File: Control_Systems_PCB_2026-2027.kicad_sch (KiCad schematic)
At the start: 13 parts, among them U1 STM32F446VETx, U3 MS5611-01BA

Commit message: fix(schematic): fixed the pin outs
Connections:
- net SPI2_CLK: now also U1.64 (PC7); no longer U1.52 (PB13)
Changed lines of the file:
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@@
+	(wire
+		(pts
+			(xy 124.46 160.02) (xy 129.54 160.02)
+		)
+		(stroke
+			(width 0)
+			(type default)
+		)
+	)
 	(wire
 		(pts
@@
 		(pts
 			(xy 99.06 48.26) (xy 101.6 48.26)
-		)
-		(stroke
-			(width 0)
-			(type default)
-		)
-	)
-	(wire
-		(pts
-			(xy 124.46 132.08) (xy 129.54 132.08)
 		)
 		(stroke
@@
 		)
 	)
-	(label "SPI2_CLK"
-		(at 129.54 132.08 0)
-		(effects
-			(font
-				(size 1.27 1.27)
-			)
-			(justify left bottom)
-		)
-	)
 	(label "SPI2_MISO"
 		(at 236.855 36.195 270)
@@
 		)
 	)
+	(label "SPI2_CLK"
+		(at 129.54 160.02 0)
+		(effects
+			(font
+				(size 1.27 1.27)
+			)
+			(justify left bottom)
+		)
+	)

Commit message: fix(schematic): applied PCB best practices + suggested changes)
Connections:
- net SSM renamed PD10_CS
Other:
- moved on the sheet: C10, U3

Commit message: feat: add usb-c recepticle (🤞 it's atleast somewhat correct)
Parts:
- added C11: 10n, symbol Device:C
- added C12: 100n, symbol Device:C
- added J1: USB_C_Receptacle_USB2.0_16P, symbol Connector:USB_C_Receptacle_USB2.0_16P
- added R1, R2: 5.1K, symbol Device:R
- added U2: USBLC6-2SC6, Package_TO_SOT_SMD:SOT-23-6, symbol Power_Protection:USBLC6-2SC6
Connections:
- net GND: now also C11.2, C12.2, J1.A1 (GND), J1.A12 (GND), J1.B1 (GND), J1.B12 (GND), J1.SH (SHIELD), R1.1, R2.2, U2.2 (GND)
- net PD10_CS: now also U1.18 (PC3); no longer U1.55 (PD8)
- net SPI2_MISO: now also U1.17 (PC2); no longer U1.53 (PB14)
- net SPI2_MOSI: now also U1.16 (PC1); no longer U1.54 (PB15)
- new net: J1.A5 (CC1), R1.2
- new net: J1.B5 (CC2), R2.1
- new net +5V: C11.1, C12.1, J1.A4 (VBUS), J1.A9 (VBUS), J1.B4 (VBUS), J1.B9 (VBUS), U2.5 (VBUS)
- new net D+STM: U1.54 (PB15), U2.6 (I/O1)
- new net D+TVS: J1.A6 (D+), J1.B6 (D+), U2.1 (I/O1)
- new net D-STM: U1.53 (PB14), U2.4 (I/O2)
- new net D-TVS: J1.A7 (D-), J1.B7 (D-), U2.3 (I/O2)
- no-connect marks 0 -> 2
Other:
- note added: "Barometer (MS5611)"
- note added: "USB_C_Recepticle"

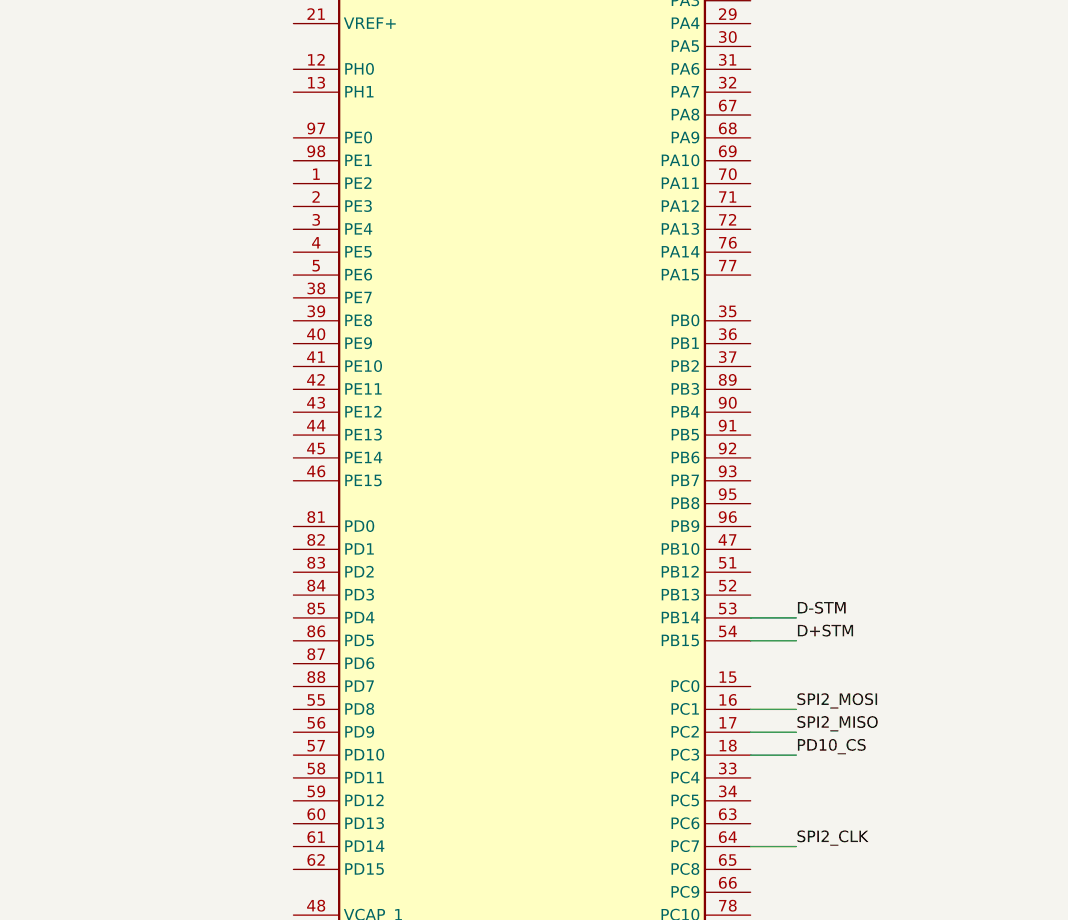
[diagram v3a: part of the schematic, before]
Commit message: fix: fixed incorrect pins usage and routed the DP/DM
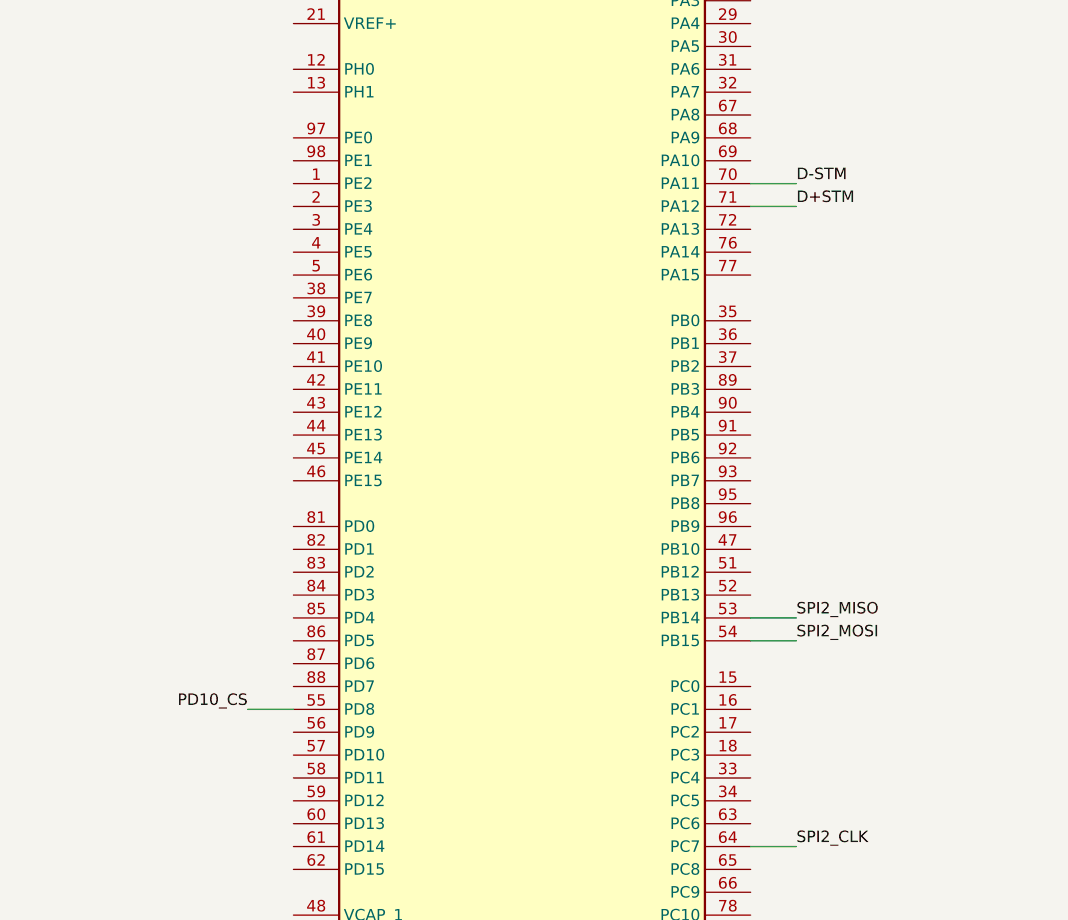
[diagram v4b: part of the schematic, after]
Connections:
- net D+STM: now also U1.71 (PA12); no longer U1.54 (PB15)
- net D-STM: now also U1.70 (PA11); no longer U1.53 (PB14)
- net PD10_CS: now also U1.55 (PD8); no longer U1.18 (PC3)
- net SPI2_MISO: now also U1.53 (PB14); no longer U1.17 (PC2)
- net SPI2_MOSI: now also U1.54 (PB15); no longer U1.16 (PC1)

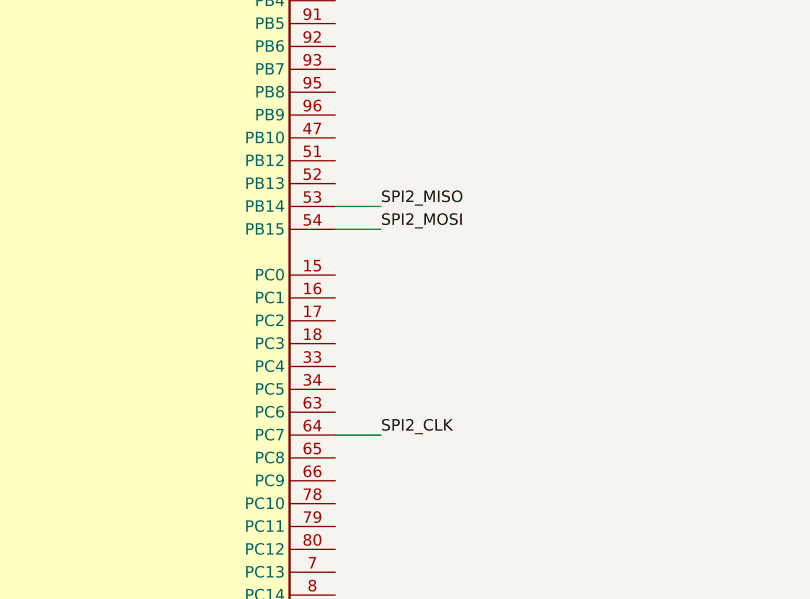
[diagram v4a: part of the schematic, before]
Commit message: fix: reroute barometer to PB13, used the wrong pin due to misunderstanding
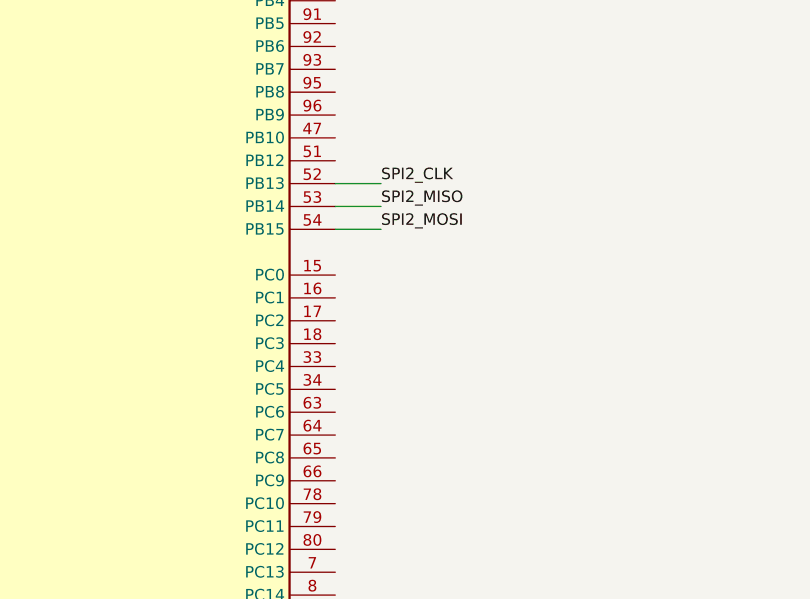
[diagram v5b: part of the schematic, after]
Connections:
- net SPI2_CLK: now also U1.52 (PB13); no longer U1.64 (PC7)
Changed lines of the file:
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@@
+		)
+	)
+	(wire
+		(pts
+			(xy 123.19 133.35) (xy 128.27 133.35)
+		)
+		(stroke
+			(width 0)
+			(type default)
 		)
 	)
@@
 		(pts
 			(xy 339.09 40.64) (xy 339.09 44.45)
-		)
-		(stroke
-			(width 0)
-			(type default)
-		)
-	)
-	(wire
-		(pts
-			(xy 123.19 161.29) (xy 128.27 161.29)
 		)
 		(stroke
@@
 	)
 	(label "SPI2_CLK"
-		(at 128.27 161.29 0)
-		(effects
-			(font
+		(at 128.27 133.35 0)
+		(effects
+			(font

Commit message: fix: remove decoupling caps on voltage line
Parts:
- removed C11: 10n, symbol Device:C
- removed C12: 100n, symbol Device:C
